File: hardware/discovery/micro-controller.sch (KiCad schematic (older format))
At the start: 3 parts, among them U4 STM32F407VG

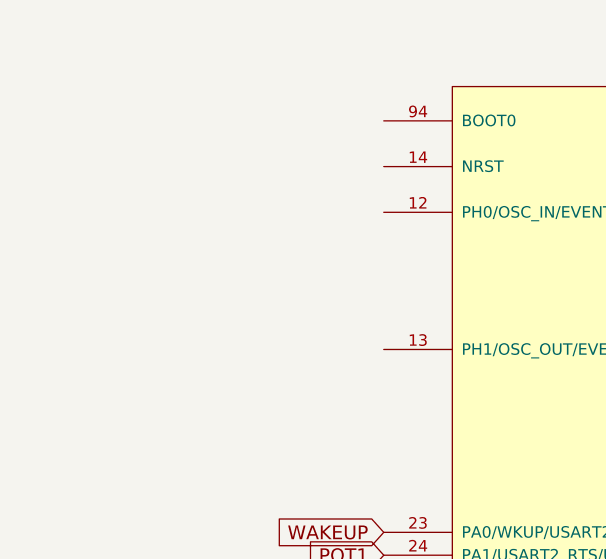
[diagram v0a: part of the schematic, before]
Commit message: Discovery: add crystal
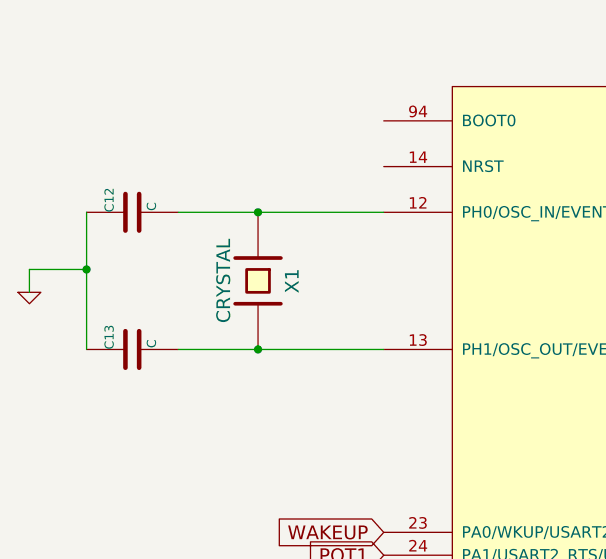
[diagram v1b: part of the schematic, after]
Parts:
- added C12, C13: C, Capacitors_SMD:C_0805, symbol C
- added X1: CRYSTAL, Crystals:Crystal_HC49-U_Vertical, symbol CRYSTAL
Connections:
- net GND: now also C12.1, C13.1
- net at U4.12 (PH0/OSC_IN/EVENTOUT): now also C12.2, X1.1
- net at U4.13 (PH1/OSC_OUT/EVENTOUT): now also C13.2, X1.2
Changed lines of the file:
@@
 Text GLabel 2850 4100 0    60   Input ~ 0
 WAKEUP
+$Comp
+L CRYSTAL X1
+U 1 1 585F8666
+P 2300 3000
+F 0 "X1" H 2300 3150 60  0000 C CNN
+F 1 "CRYSTAL" H 2300 2850 60  0000 C CNN
+F 2 "Crystals:Crystal_HC49-U_Vertical" H 2300 3000 60  0001 C CNN
+F 3 "" H 2300 3000 60  0000 C CNN
+	1    2300 3000
+	0    1    1    0
+$EndComp
+Wire Wire Line
+	1950 2700 2850 2700
+Wire Wire Line
+	1950 3300 2850 3300
+$Comp
+L C C12
+U 1 1 585F8833
+P 1750 2700
+F 0 "C12" H 1750 2800 40  0000 L CNN
+F 1 "C" H 1756 2615 40  0000 L CNN
+F 2 "Capacitors_SMD:C_0805" H 1788 2550 30  0001 C CNN
+F 3 "" H 1750 2700 60  0000 C CNN
+	1    1750 2700
+	0    -1   -1   0
+$EndComp
+$Comp
+L C C13
+U 1 1 585F888D
+P 1750 3300
+F 0 "C13" H 1750 3400 40  0000 L CNN
+F 1 "C" H 1756 3215 40  0000 L CNN
+F 2 "Capacitors_SMD:C_0805" H 1788 3150 30  0001 C CNN
+F 3 "" H 1750 3300 60  0000 C CNN
+	1    1750 3300
+	0    -1   -1   0
+$EndComp
+Connection ~ 2300 2700
+Connection ~ 2300 3300
+Wire Wire Line
+	1550 3300 1550 2700
+Wire Wire Line
+	1550 2950 1300 2950
+Wire Wire Line
+	1300 2950 1300 3050
+Connection ~ 1550 2950
+$Comp
+L GND #PWR020
+U 1 1 585F8908
+P 1300 3050
+F 0 "#PWR020" H 1300 3050 30  0001 C CNN
+F 1 "GND" H 1300 2980 30  0001 C CNN
+F 2 "" H 1300 3050 60  0001 C CNN
+F 3 "" H 1300 3050 60  0001 C CNN
+	1    1300 3050
+	1    0    0    -1
+$EndComp
 $EndSCHEMATC

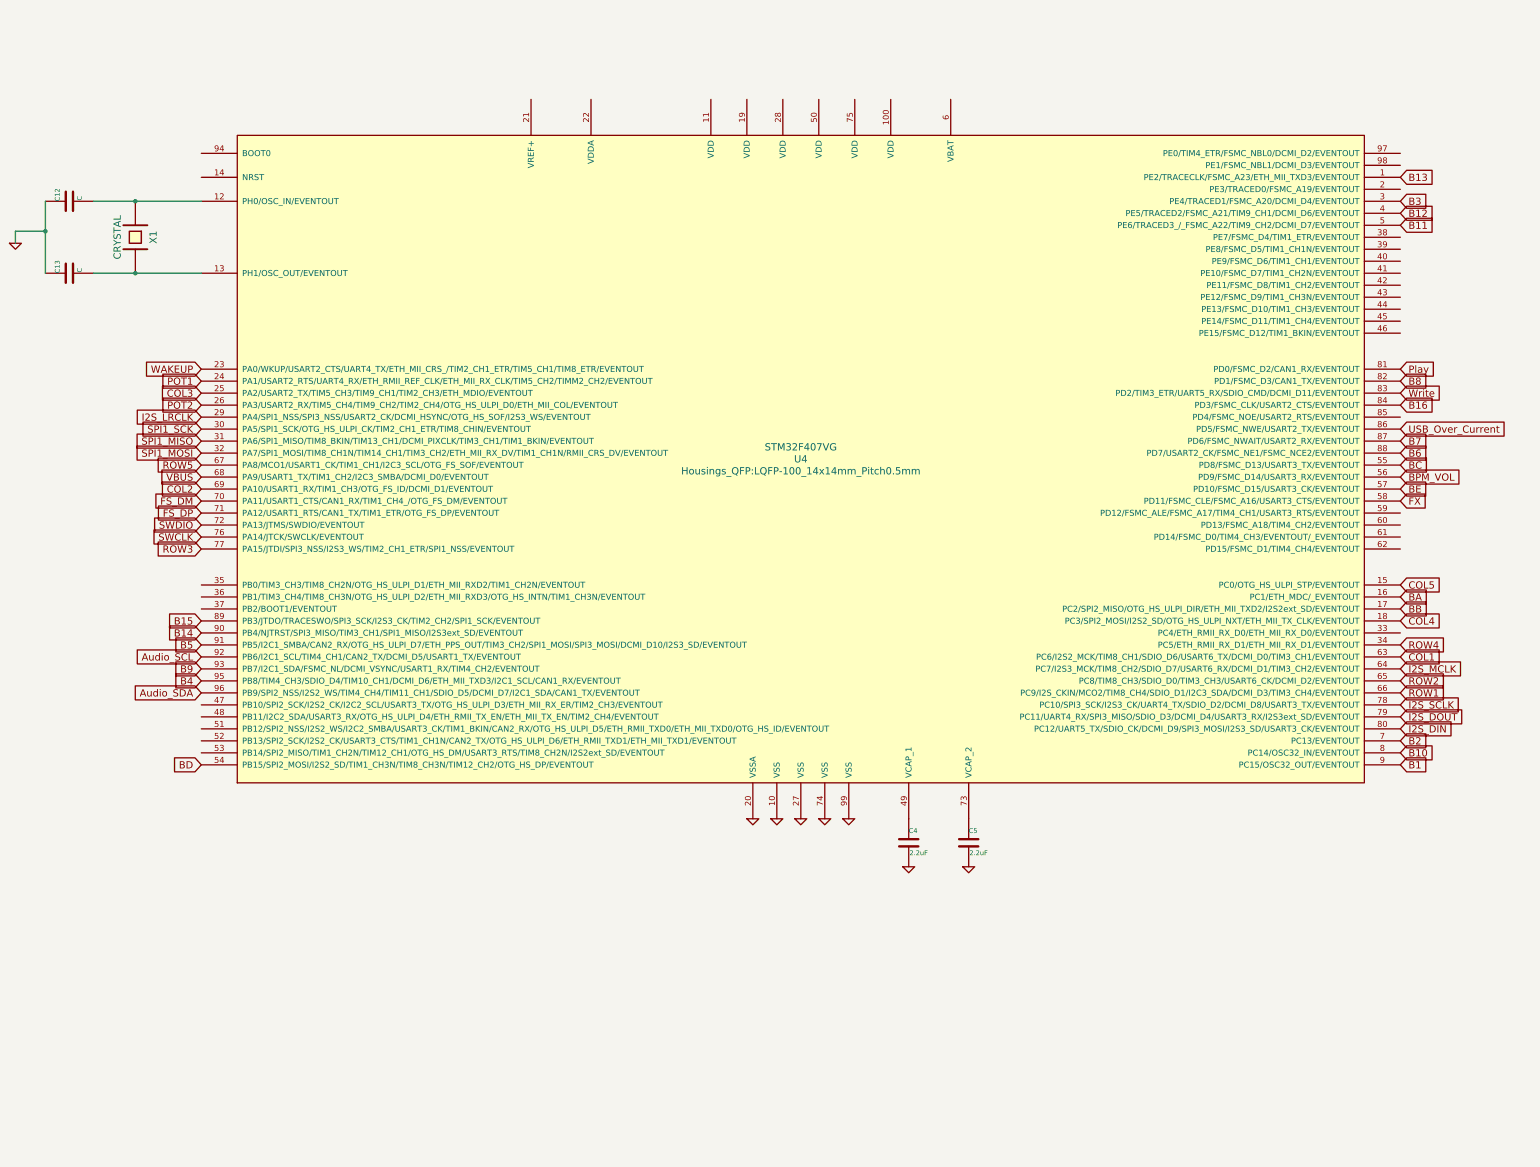
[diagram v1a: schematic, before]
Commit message: Discovery: STM32F4 power a filtering
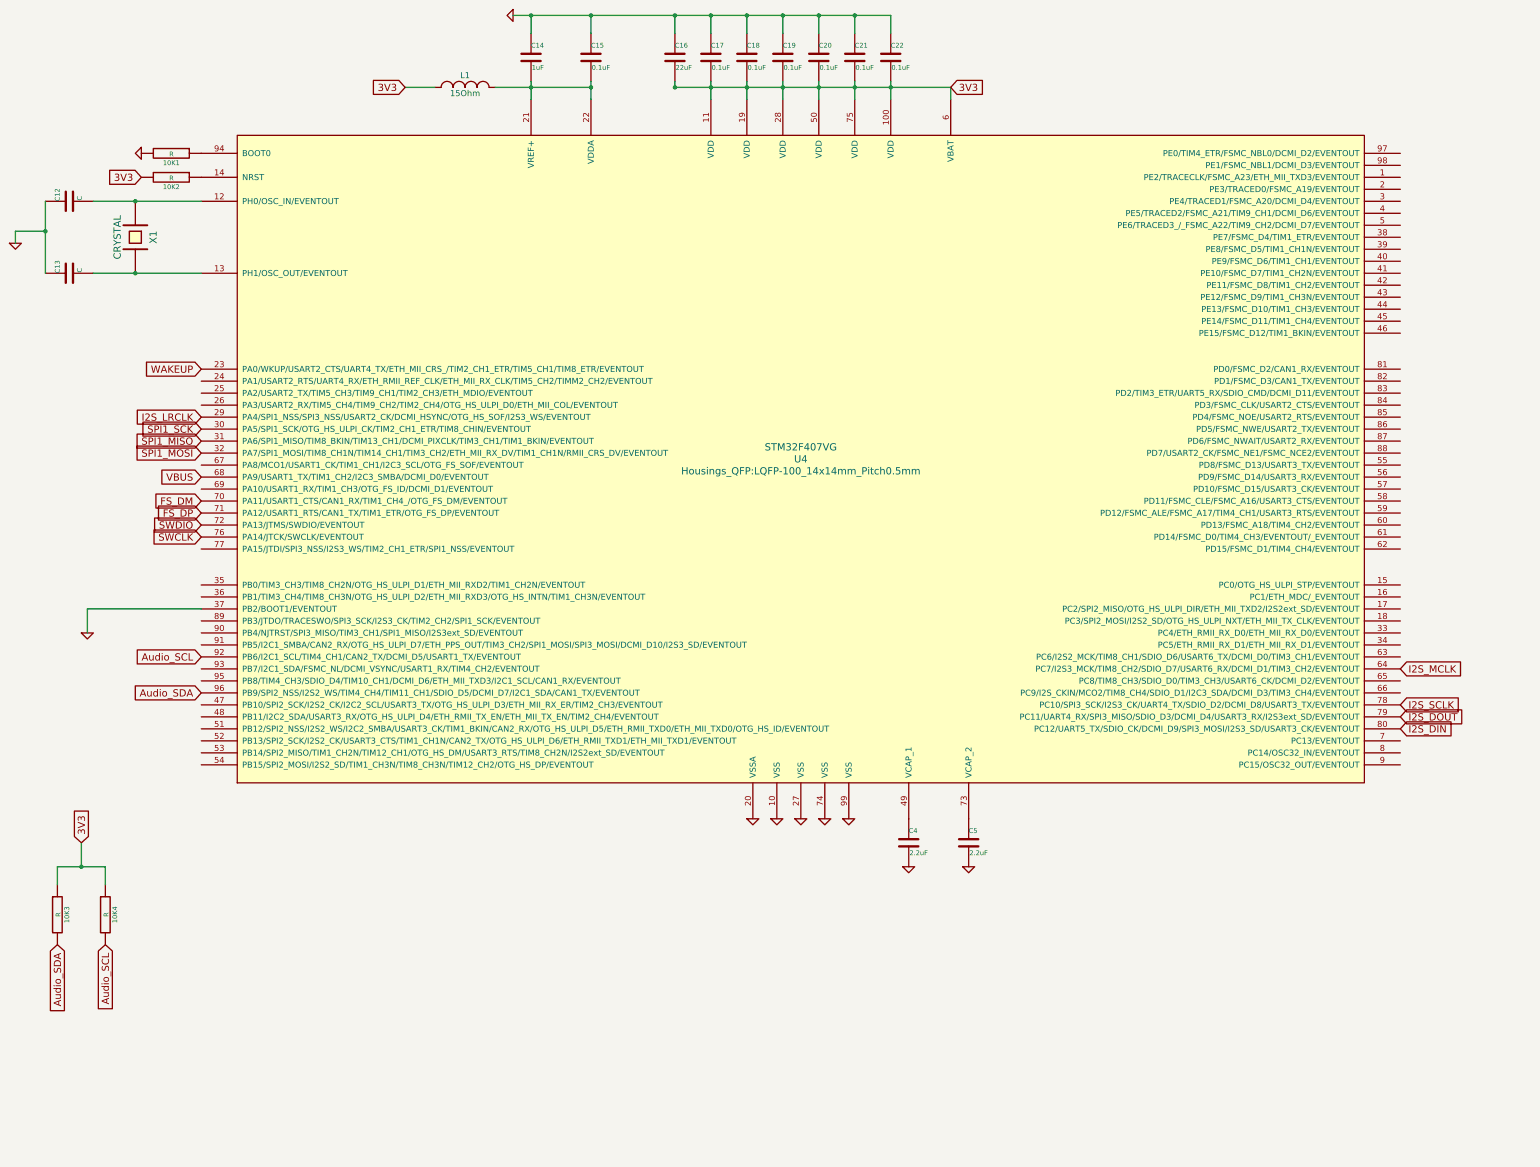
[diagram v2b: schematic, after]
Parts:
- added 10K1, 10K2, 10K3, 10K4: R, symbol R
- added C14: 1uF, Capacitors_SMD:C_0805, symbol C
- added C15, C17, C18, C19, C20, C21, C22: 0.1uF, Capacitors_SMD:C_0805, symbol C
- added C16: 22uF, Capacitors_SMD:C_0805, symbol C
- added L1: 15Ohm, Resistors_SMD:R_0805, symbol INDUCTOR_SMALL
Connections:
- net Audio_SCL: now also 10K4.2
- net Audio_SDA: now also 10K3.2
- net GND: now also U4.37 (PB2/BOOT1/EVENTOUT), 10K1.2, C14.1, C15.1, C16.1, C17.1, C18.1, C19.1, C20.1, C21.1, C22.1
- net 3V3: now reaches U4.100 (VDD)
- net 3V3: now also U4.11 (VDD), U4.19 (VDD), U4.28 (VDD), U4.50 (VDD), U4.6 (VBAT), U4.75 (VDD), 10K2.2, 10K3.1, 10K4.1, C16.2, C17.2, C18.2, C19.2, C20.2, C21.2, C22.2, L1.1
- net at U4.14 (NRST): now also 10K2.1
- net at U4.21 (VREF+): now also U4.22 (VDDA), C14.2, C15.2, L1.2
- net at U4.94 (BOOT0): now also 10K1.1
- net B1: no longer names the net of U4.9 (PC15/OSC32_OUT/EVENTOUT)
- net B10: no longer names the net of U4.8 (PC14/OSC32_IN/EVENTOUT)
- net B11: no longer names the net of U4.5 (PE6/TRACED3_/_FSMC_A22/TIM9_CH2/DCMI_D7/EVENTOUT)
- net B12: no longer names the net of U4.4 (PE5/TRACED2/FSMC_A21/TIM9_CH1/DCMI_D6/EVENTOUT)
- net B13: no longer names the net of U4.1 (PE2/TRACECLK/FSMC_A23/ETH_MII_TXD3/EVENTOUT)
- net B14: no longer names the net of U4.90 (PB4/NJTRST/SPI3_MISO/TIM3_CH1/SPI1_MISO/I2S3ext_SD/EVENTOUT)
- net B15: no longer names the net of U4.89 (PB3/JTDO/TRACESWO/SPI3_SCK/I2S3_CK/TIM2_CH2/SPI1_SCK/EVENTOUT)
- net B16: no longer names the net of U4.84 (PD3/FSMC_CLK/USART2_CTS/EVENTOUT)
- net B2: no longer names the net of U4.7 (PC13/EVENTOUT)
- net B3: no longer names the net of U4.3 (PE4/TRACED1/FSMC_A20/DCMI_D4/EVENTOUT)
- net B4: no longer names the net of U4.95 (PB8/TIM4_CH3/SDIO_D4/TIM10_CH1/DCMI_D6/ETH_MII_TXD3/I2C1_SCL/CAN1_RX/EVENTOUT)
- net B5: no longer names the net of U4.91 (PB5/I2C1_SMBA/CAN2_RX/OTG_HS_ULPI_D7/ETH_PPS_OUT/TIM3_CH2/SPI1_MOSI/SPI3_MOSI/DCMI_D10/I2S3_SD/EVENTOUT)
- net B6: no longer names the net of U4.88 (PD7/USART2_CK/FSMC_NE1/FSMC_NCE2/EVENTOUT)
- net B7: no longer names the net of U4.87 (PD6/FSMC_NWAIT/USART2_RX/EVENTOUT)
- net B8: no longer names the net of U4.82 (PD1/FSMC_D3/CAN1_TX/EVENTOUT)
- net B9: no longer names the net of U4.93 (PB7/I2C1_SDA/FSMC_NL/DCMI_VSYNC/USART1_RX/TIM4_CH2/EVENTOUT)
- net BA: no longer names the net of U4.16 (PC1/ETH_MDC/_EVENTOUT)
- net BB: no longer names the net of U4.17 (PC2/SPI2_MISO/OTG_HS_ULPI_DIR/ETH_MII_TXD2/I2S2ext_SD/EVENTOUT)
- net BC: no longer names the net of U4.55 (PD8/FSMC_D13/USART3_TX/EVENTOUT)
- net BD: no longer names the net of U4.54 (PB15/SPI2_MOSI/I2S2_SD/TIM1_CH3N/TIM8_CH3N/TIM12_CH2/OTG_HS_DP/EVENTOUT)
- net BE: no longer names the net of U4.57 (PD10/FSMC_D15/USART3_CK/EVENTOUT)
- net BPM_VOL: no longer names the net of U4.56 (PD9/FSMC_D14/USART3_RX/EVENTOUT)
- net COL1: no longer names the net of U4.63 (PC6/I2S2_MCK/TIM8_CH1/SDIO_D6/USART6_TX/DCMI_D0/TIM3_CH1/EVENTOUT)
- net COL2: no longer names the net of U4.69 (PA10/USART1_RX/TIM1_CH3/OTG_FS_ID/DCMI_D1/EVENTOUT)
- net COL3: no longer names the net of U4.25 (PA2/USART2_TX/TIM5_CH3/TIM9_CH1/TIM2_CH3/ETH_MDIO/EVENTOUT)
- net COL4: no longer names the net of U4.18 (PC3/SPI2_MOSI/I2S2_SD/OTG_HS_ULPI_NXT/ETH_MII_TX_CLK/EVENTOUT)
- net COL5: no longer names the net of U4.15 (PC0/OTG_HS_ULPI_STP/EVENTOUT)
- net FX: no longer names the net of U4.58 (PD11/FSMC_CLE/FSMC_A16/USART3_CTS/EVENTOUT)
- net POT1: no longer names the net of U4.24 (PA1/USART2_RTS/UART4_RX/ETH_RMII_REF_CLK/ETH_MII_RX_CLK/TIM5_CH2/TIMM2_CH2/EVENTOUT)
- net POT2: no longer names the net of U4.26 (PA3/USART2_RX/TIM5_CH4/TIM9_CH2/TIM2_CH4/OTG_HS_ULPI_D0/ETH_MII_COL/EVENTOUT)
- net Play: no longer names the net of U4.81 (PD0/FSMC_D2/CAN1_RX/EVENTOUT)
- net ROW1: no longer names the net of U4.66 (PC9/I2S_CKIN/MCO2/TIM8_CH4/SDIO_D1/I2C3_SDA/DCMI_D3/TIM3_CH4/EVENTOUT)
- net ROW2: no longer names the net of U4.65 (PC8/TIM8_CH3/SDIO_D0/TIM3_CH3/USART6_CK/DCMI_D2/EVENTOUT)
- net ROW3: no longer names the net of U4.77 (PA15/JTDI/SPI3_NSS/I2S3_WS/TIM2_CH1_ETR/SPI1_NSS/EVENTOUT)
- net ROW4: no longer names the net of U4.34 (PC5/ETH_RMII_RX_D1/ETH_MII_RX_D1/EVENTOUT)
- net ROW5: no longer names the net of U4.67 (PA8/MCO1/USART1_CK/TIM1_CH1/I2C3_SCL/OTG_FS_SOF/EVENTOUT)
- net USB_Over_Current: no longer names the net of U4.86 (PD5/FSMC_NWE/USART2_TX/EVENTOUT)
- net Write: no longer names the net of U4.83 (PD2/TIM3_ETR/UART5_RX/SDIO_CMD/DCMI_D11/EVENTOUT)

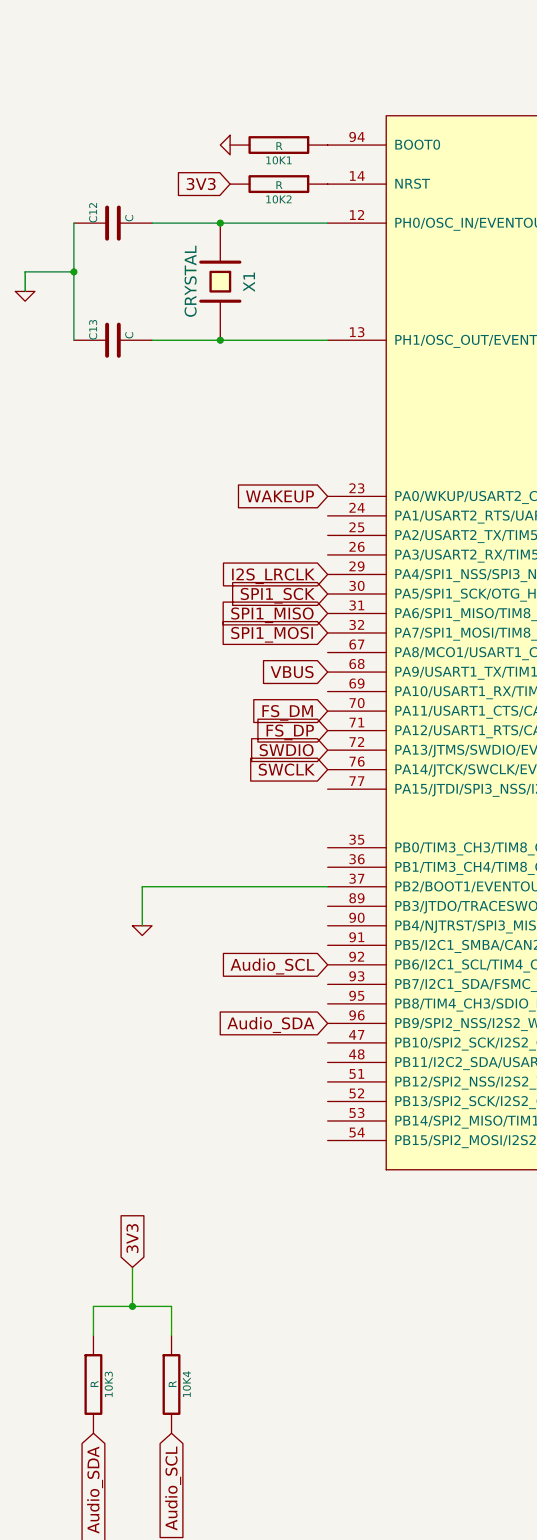
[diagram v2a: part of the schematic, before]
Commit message: Discovery: Fix pull-ups and add LED current limiters
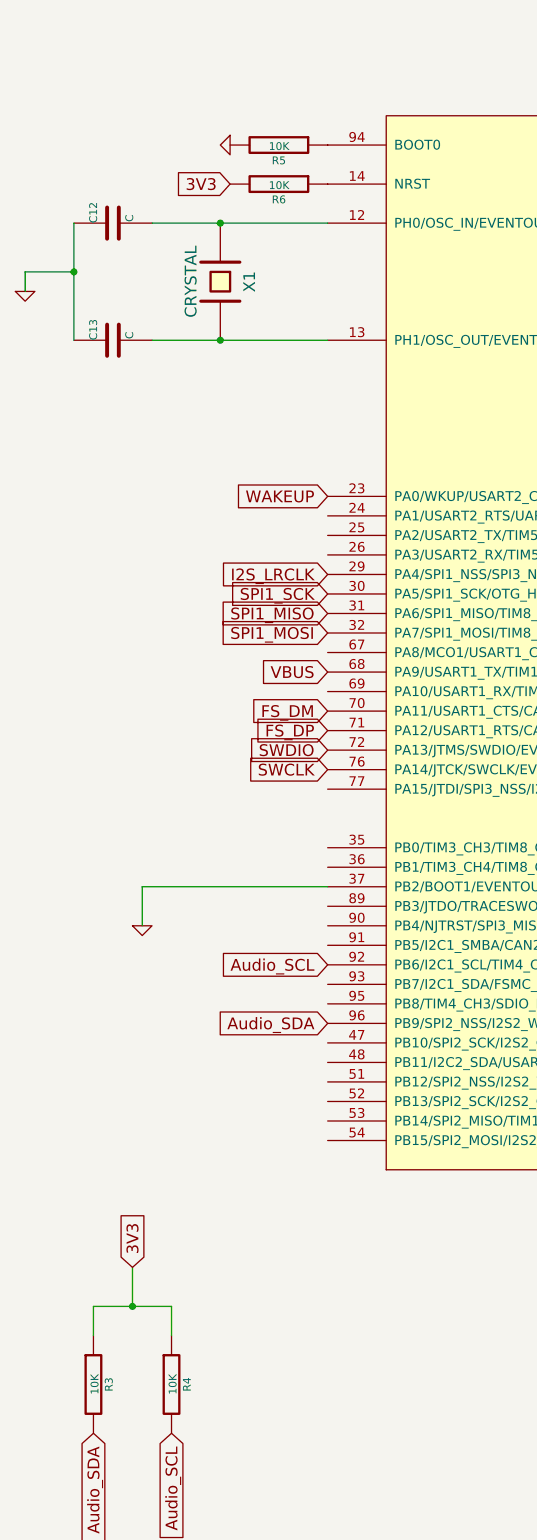
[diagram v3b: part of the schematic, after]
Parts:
- L1: footprint Resistors_SMD:R_0805 -> Capacitors_SMD:C_0805
- R3: renamed from 10K3; value R -> 10K; footprint (none) -> Resistors_SMD:R_0805
- R4: renamed from 10K4; value R -> 10K; footprint (none) -> Resistors_SMD:R_0805
- R5: renamed from 10K1; value R -> 10K; footprint (none) -> Resistors_SMD:R_0805
- R6: renamed from 10K2; value R -> 10K; footprint (none) -> Resistors_SMD:R_0805
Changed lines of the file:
@@
 F 0 "L1" H 5050 1850 50  0000 C CNN
 F 1 "15Ohm" H 5050 1700 50  0000 C CNN
-F 2 "Resistors_SMD:R_0805" H 5050 1750 60  0001 C CNN
+F 2 "Capacitors_SMD:C_0805" H 5050 1750 60  0001 C CNN
 F 3 "" H 5050 1750 60  0000 C CNN
 	1    5050 1750
@@
 3V3
 $Comp
-L R 10K1
+L R R5
 U 1 1 58612338
 P 2600 2300
-F 0 "10K1" V 2680 2300 40  0000 C CNN
-F 1 "R" V 2607 2301 40  0000 C CNN
-F 2 "" V 2530 2300 30  0001 C CNN
+F 0 "R5" V 2680 2300 40  0000 C CNN
+F 1 "10K" V 2607 2301 40  0000 C CNN
+F 2 "Resistors_SMD:R_0805" V 2530 2300 30  0001 C CNN
 F 3 "" H 2600 2300 30  0000 C CNN
 	1    2600 2300
@@
 $EndComp
 $Comp
-L R 10K2
+L R R6
 U 1 1 586123C6
 P 2600 2500
-F 0 "10K2" V 2680 2500 40  0000 C CNN
-F 1 "R" V 2607 2501 40  0000 C CNN
-F 2 "" V 2530 2500 30  0001 C CNN
+F 0 "R6" V 2680 2500 40  0000 C CNN
+F 1 "10K" V 2607 2501 40  0000 C CNN
+F 2 "Resistors_SMD:R_0805" V 2530 2500 30  0001 C CNN
 F 3 "" H 2600 2500 30  0000 C CNN
 	1    2600 2500
@@
 3V3
 $Comp
-L R 10K3
+L R R3
 U 1 1 586150DA
 P 1650 8650
-F 0 "10K3" V 1730 8650 40  0000 C CNN
-F 1 "R" V 1657 8651 40  0000 C CNN
-F 2 "" V 1580 8650 30  0001 C CNN
+F 0 "R3" V 1730 8650 40  0000 C CNN
+F 1 "10K" V 1657 8651 40  0000 C CNN
+F 2 "Resistors_SMD:R_0805" V 1580 8650 30  0001 C CNN
 F 3 "" H 1650 8650 30  0000 C CNN
 	1    1650 8650
@@
 $EndComp
 $Comp
-L R 10K4
+L R R4
 U 1 1 58615169
 P 2050 8650
-F 0 "10K4" V 2130 8650 40  0000 C CNN
-F 1 "R" V 2057 8651 40  0000 C CNN
-F 2 "" V 1980 8650 30  0001 C CNN
+F 0 "R4" V 2130 8650 40  0000 C CNN
+F 1 "10K" V 2057 8651 40  0000 C CNN
+F 2 "Resistors_SMD:R_0805" V 1980 8650 30  0001 C CNN
 F 3 "" H 2050 8650 30  0000 C CNN
 	1    2050 8650
